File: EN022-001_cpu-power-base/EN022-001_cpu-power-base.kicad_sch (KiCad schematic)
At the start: 20 parts, among them J10 GBA_Slot, J3 CART SLOT TOP ROW, J4 CART SLOT FRONT ROW, J7 Conn_01x07, J8 EXP2, J9 EXP1, M2_1 Screw_Terminal_01x01, M2_2 Screw_Terminal_01x01, M2_3 Screw_Terminal_01x01, M2_4 Screw_Terminal_01x01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

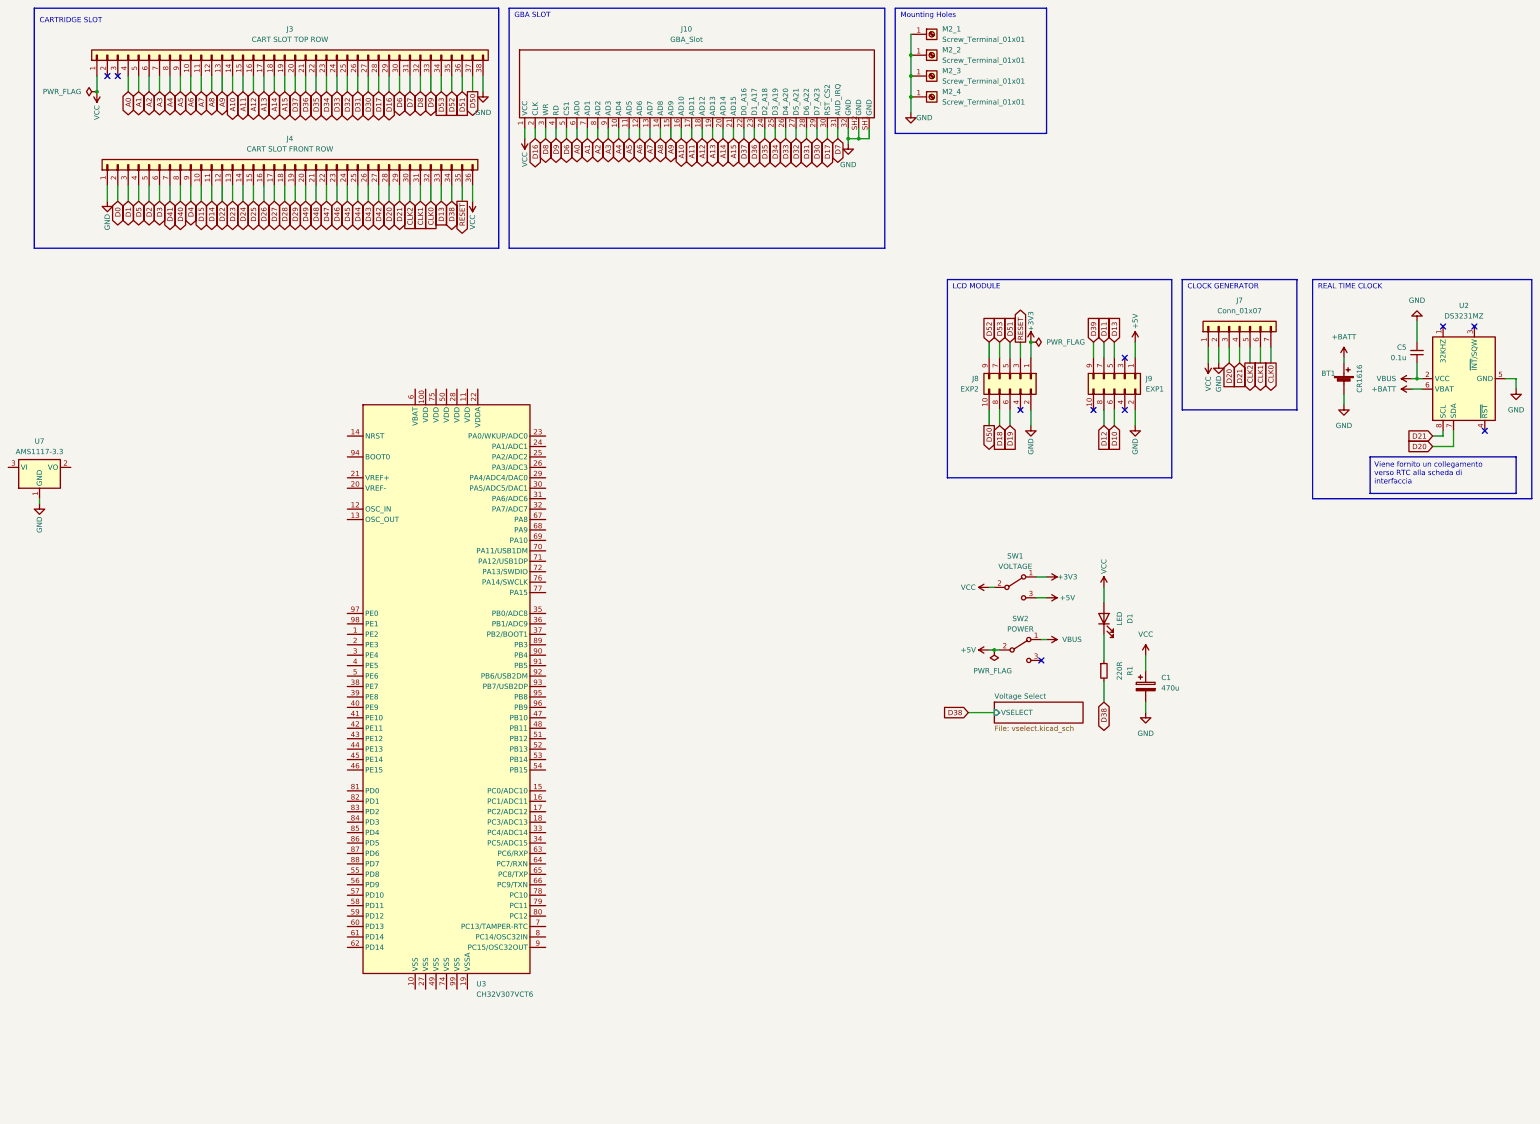
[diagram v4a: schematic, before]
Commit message: first cimplete  version of CPU POWER BASE
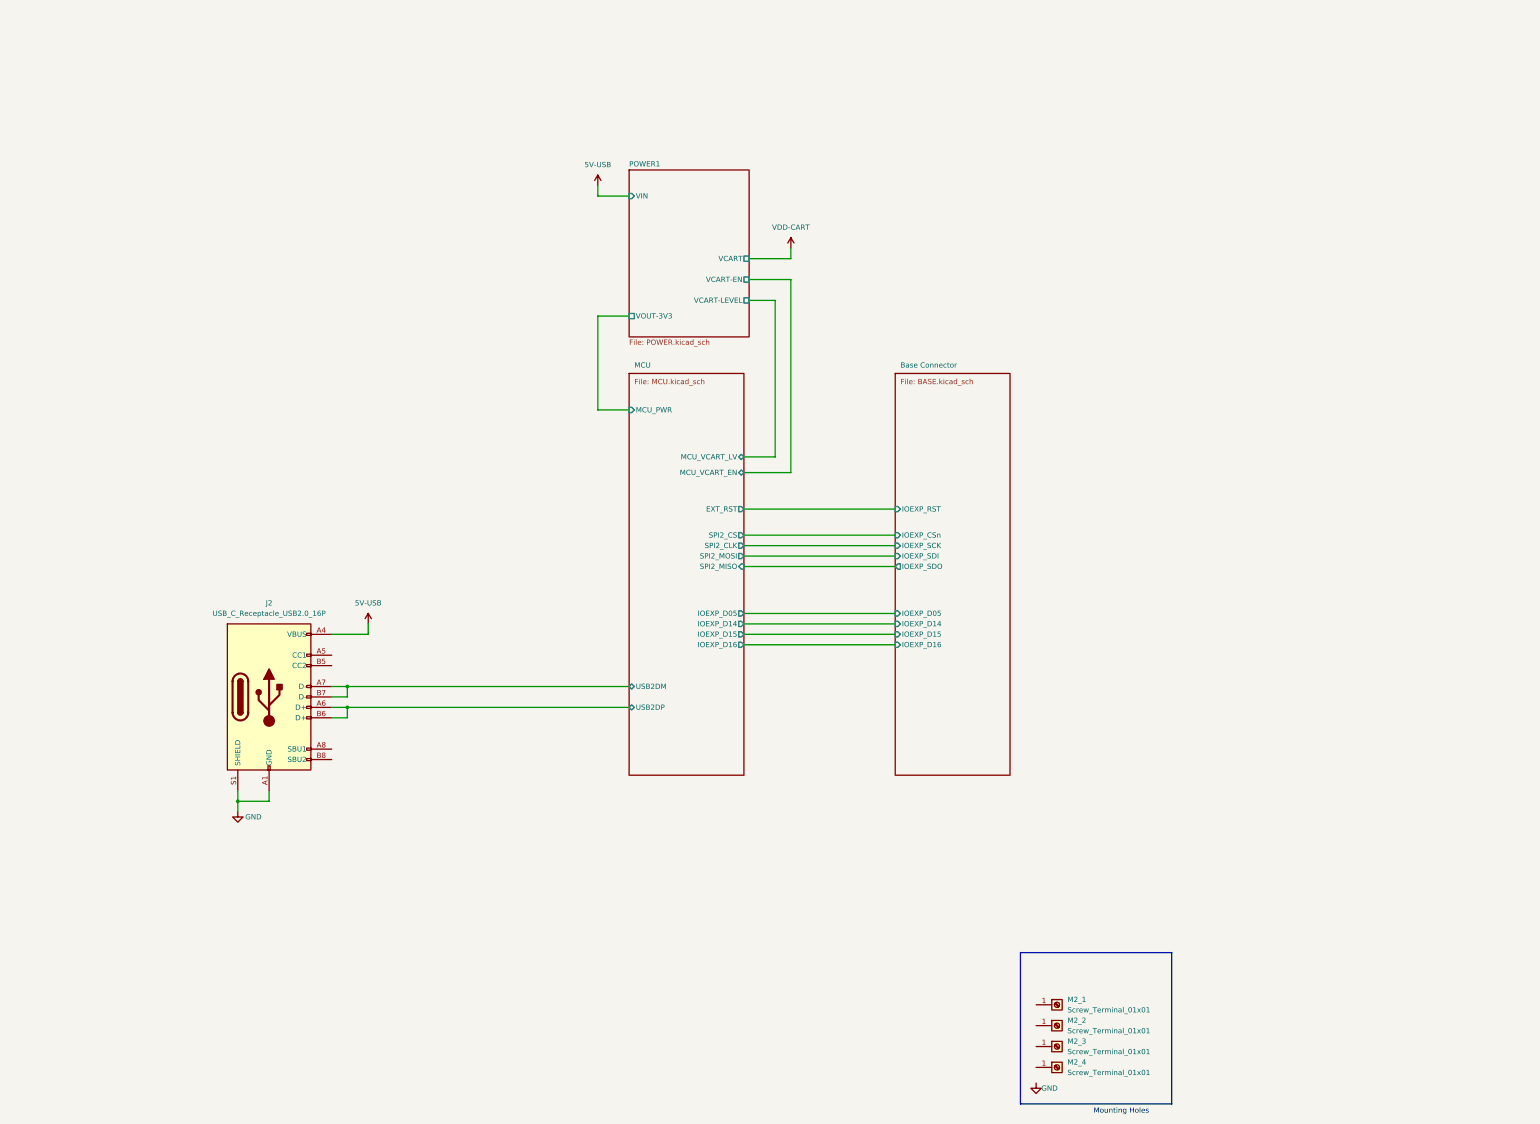
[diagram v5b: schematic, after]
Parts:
- removed BT1: CR1616, !OSCR:CR1616, symbol Device:Battery_Cell
- removed C1: 470u, Capacitor_THT:CP_Radial_D8.0mm_P3.50mm, symbol Device:C_Polarized
- removed C5: 0.1u, Capacitor_SMD:C_0402_1005Metric_Pad0.74x0.62mm_HandSolder, symbol Device:C_Small
- removed D1: LED, LED_THT:LED_D3.0mm, symbol Device:LED
- removed J10: GBA_Slot, !OSCR:GBA_Slot, symbol !OSCR:GBA_Slot
- removed J3: CART SLOT TOP ROW, !OSCR:Cartridge_Port_Adapter-Back, symbol Connector_Generic:Conn_01x38
- removed J4: CART SLOT FRONT ROW, !OSCR:Cartridge_Port_Adapter-Front, symbol Connector_Generic:Conn_01x36
- removed J7: Conn_01x07, !OSCR:Clock_Generator_Header, symbol Connector_Generic:Conn_01x07
- removed J8: EXP2, !OSCR:LCD_Header, symbol Connector_Generic:Conn_02x05_Odd_Even
- removed J9: EXP1, !OSCR:LCD_Header, symbol Connector_Generic:Conn_02x05_Odd_Even
- removed R1: 220R, Resistor_THT:R_Axial_DIN0207_L6.3mm_D2.5mm_P10.16mm_Horizontal, symbol Device:R_Small
- removed SW1: VOLTAGE, !OSCR:Power_Switch, symbol Switch:SW_SPDT
- removed SW2: POWER, !OSCR:Power_Switch, symbol Switch:SW_SPDT
- removed U2: DS3231MZ, Package_SO:SOIC-8_3.9x4.9mm_P1.27mm, symbol Timer_RTC:DS3231MZ
- removed U3: CH32V307VCT6, Package_QFP:LQFP-100_14x14mm_P0.5mm, symbol wch-mcu:CH32V307VCT6
- removed U7: AMS1117-3.3, Package_TO_SOT_SMD:SOT-223-3_TabPin2, symbol Regulator_Linear:AMS1117-3.3
- added J2: USB_C_Receptacle_USB2.0_16P, Connector_USB:USB_C_Receptacle_GCT_USB4105-xx-A_16P_TopMnt_Horizontal, symbol Connector:USB_C_Receptacle_USB2.0_16P
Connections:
- net GND: now also J2.A1 (GND), J2.A12 (GND), J2.B1 (GND), J2.B12 (GND), J2.S1 (SHIELD); no longer M2_1.1 (Pin_1), M2_2.1 (Pin_1), M2_3.1 (Pin_1), M2_4.1 (Pin_1)
- new net 5V-USB: J2.A4 (VBUS), J2.A9 (VBUS), J2.B4 (VBUS), J2.B9 (VBUS)
- new net MCU/USB2DM: J2.A7 (D-), J2.B7 (D-)
- new net MCU/USB2DP: J2.A6 (D+), J2.B6 (D+)
- no-connect marks 10 -> 0
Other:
- removed sheet Voltage Select
- added sheet Base Connector (BASE.kicad_sch)
- added sheet MCU (MCU.kicad_sch)
- added sheet POWER1 (POWER.kicad_sch)
- note removed: "CARTRIDGE SLOT"
- note removed: "CLOCK GENERATOR"
- note removed: "GBA SLOT"
- note removed: "LCD MODULE"
- note removed: "REAL TIME CLOCK"
- title: Base board with CPU nad power supply -> Base board with CPU and power supply
- moved on the sheet: M2_1, M2_2, M2_3, M2_4
